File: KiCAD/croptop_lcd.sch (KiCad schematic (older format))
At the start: 73 parts, among them J4 54104-4031, U6 IS66WV51216EBLL, U7 BU21026MUV-E2

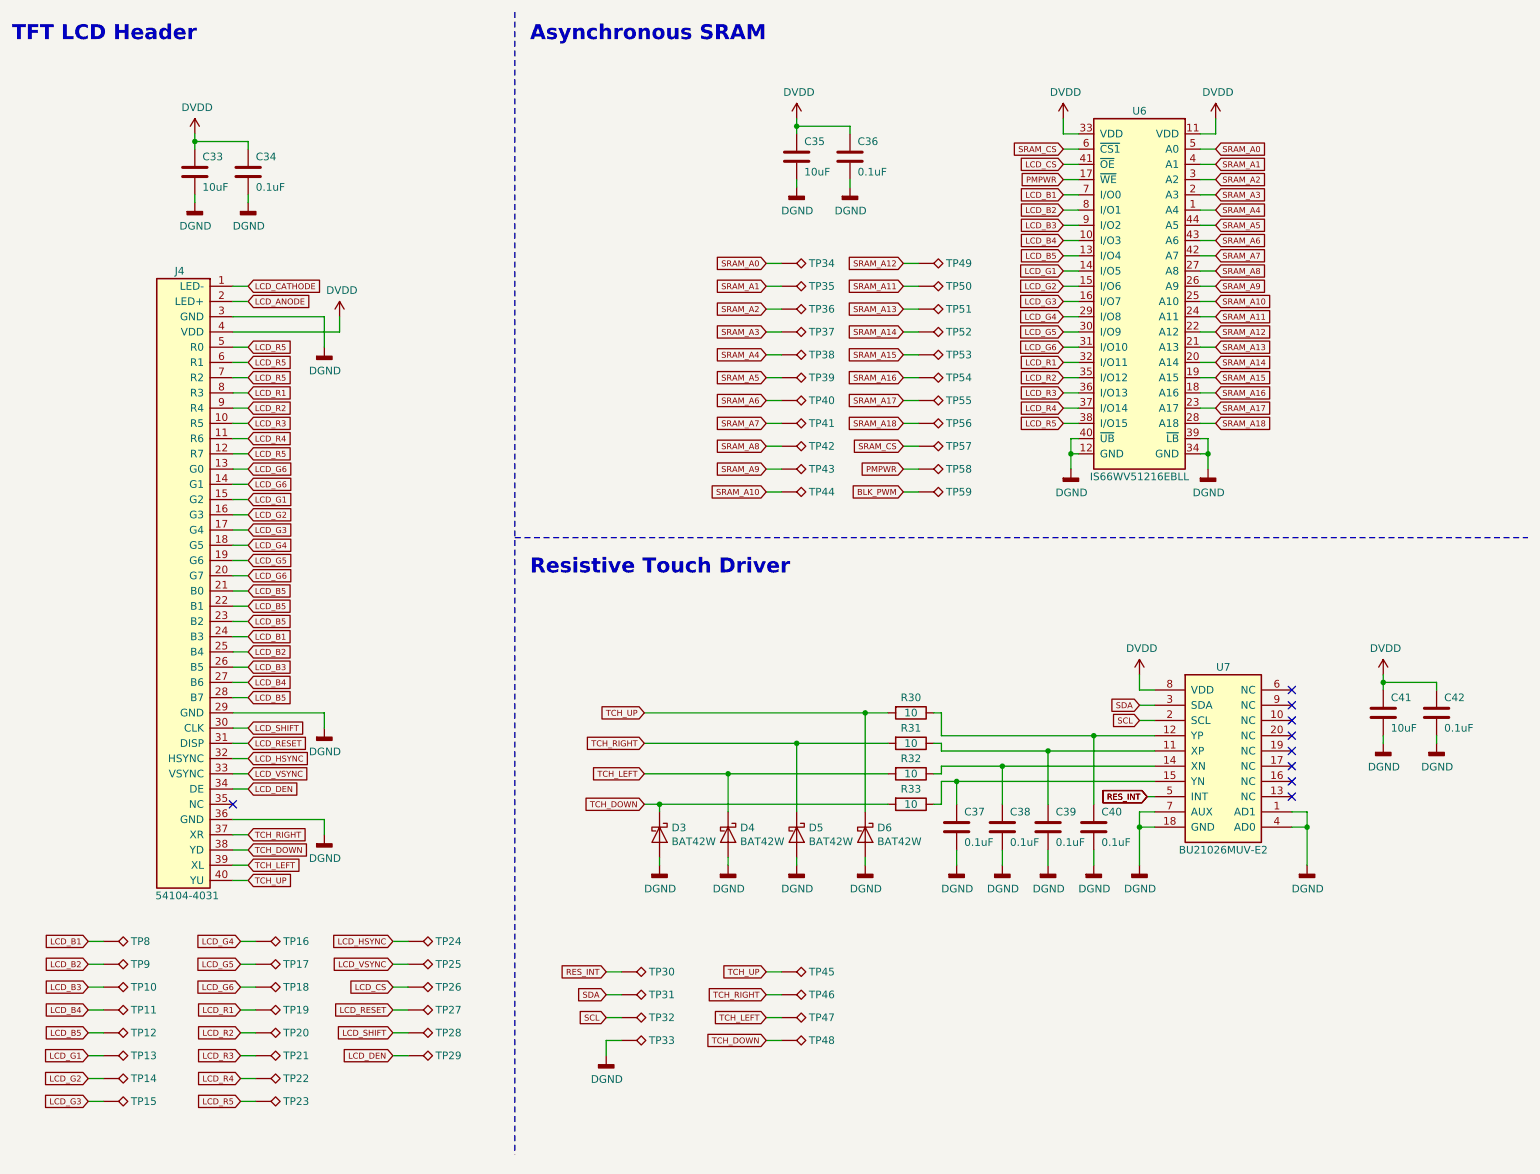
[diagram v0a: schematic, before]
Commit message: Got to PCB layout
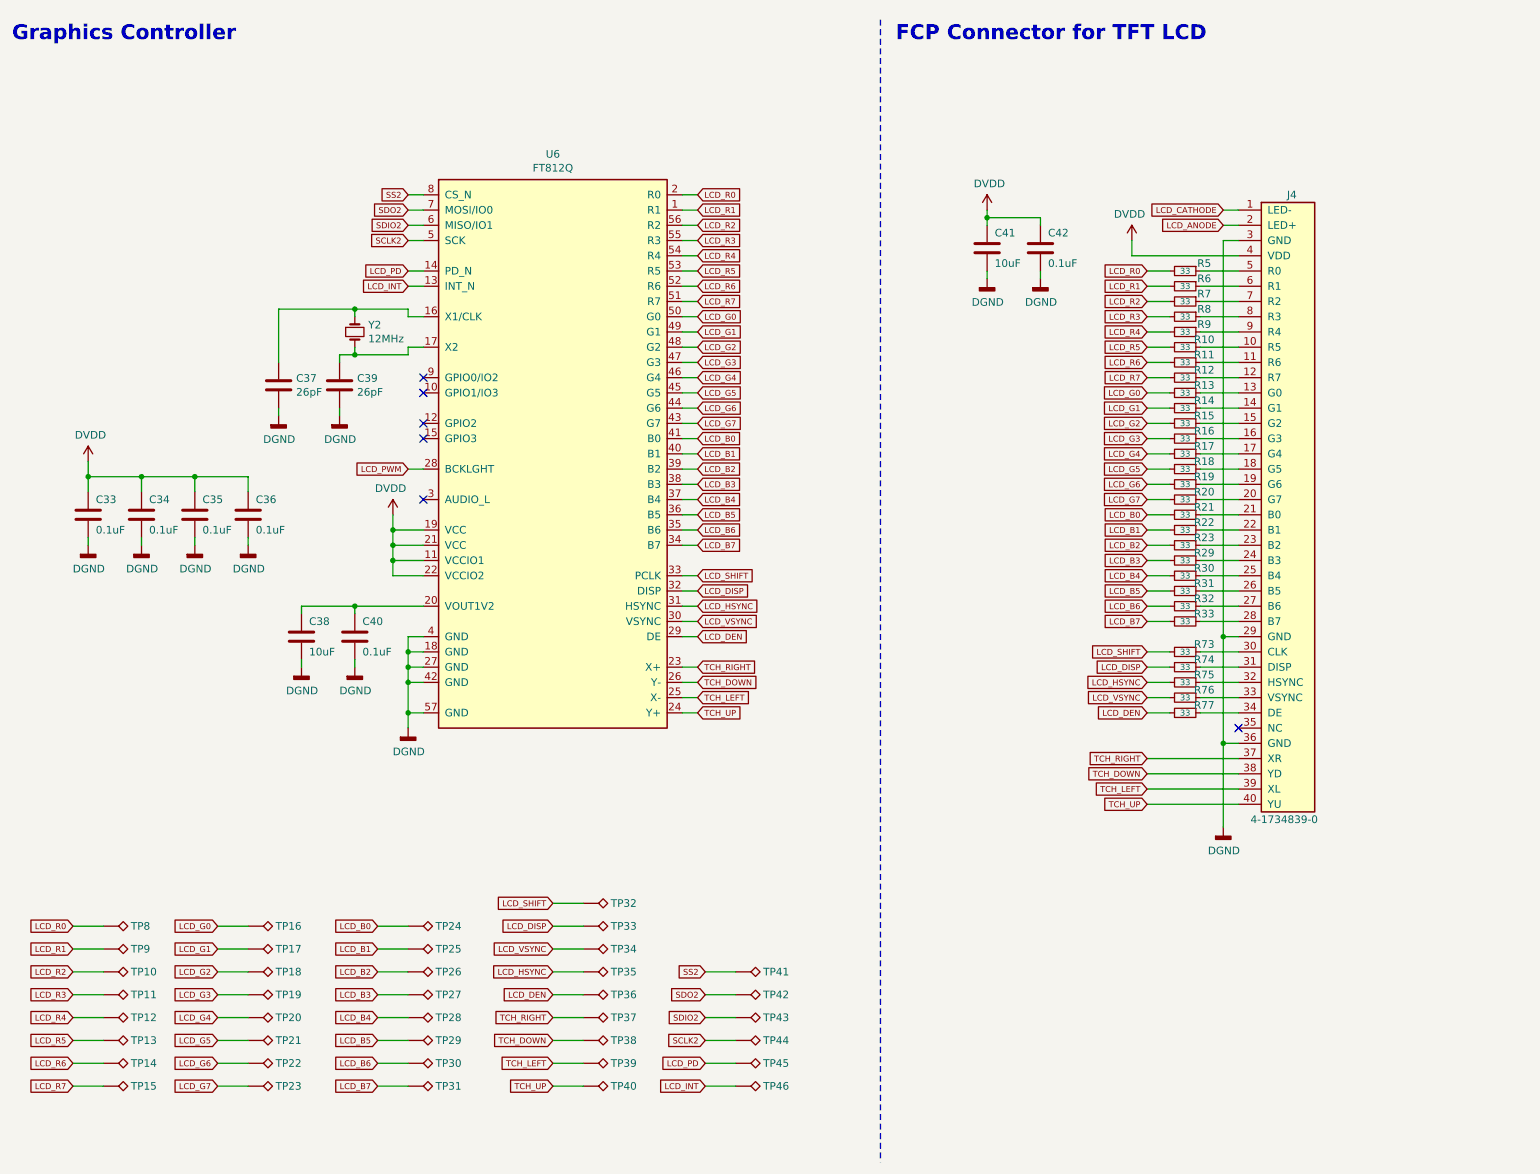
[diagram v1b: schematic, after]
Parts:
- removed D3, D4, D5, D6: BAT42W, symbol Device:D_Schottky
- removed R30, R31, R32, R33: 10, Resistor_SMD:R_0402_1005Metric, symbol Device:R
- removed TP47, TP48, TP49, TP50, TP51, TP52, TP53, TP54, TP55, TP56, TP57, TP58, TP59: TestPoint_Alt, TestPoint:TestPoint_Pad_D2.0mm, symbol Connector:TestPoint_Alt
- removed U6: IS66WV51216EBLL, Package_SO:TSOP-II-44_10.16x18.41mm_P0.8mm, symbol CropTop:IS66WV51216EBLL
- removed U7: BU21026MUV-E2, Package_DFN_QFN:VQFN-24-1EP_4x4mm_P0.5mm_EP2.45x2.45mm, symbol CropTop:BU21026MUV-E2
- added R10, R11, R12, R13, R14, R15, R16, R17, R18, R19, R20, R21, R22, R23, R29, R30, R31, R32, R33, R5, R6, R7, R73, R74, R75, R76, R77, R8, R9: 33, Resistor_SMD:R_0402_1005Metric, symbol Device:R_Small
- added U6: FT812Q, Package_DFN_QFN:QFN-56-1EP_8x8mm_P0.5mm_EP4.5x5.2mm, symbol CropTop:FT812Q
- added Y2: 12MHz, croptop:ABLS_OX, symbol Device:Crystal_Small
- C33, C35: value 10uF -> 0.1uF; footprint Capacitor_SMD:C_0805_2012Metric -> Capacitor_SMD:C_0402_1005Metric
- C37, C39: value 0.1uF -> 26pF
- C38: value 0.1uF -> 10uF; footprint Capacitor_SMD:C_0402_1005Metric -> Capacitor_SMD:C_0805_2012Metric
- J4: value 54104-4031 -> 4-1734839-0; footprint (none) -> croptop:4-1734839-0
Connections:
- net LCD_CS is gone; now on net LCD_B2: TP26.1
- net SCL is gone; now on net LCD_SHIFT: TP32.1
- net SRAM_A0 is gone; now on net LCD_VSYNC: TP34.1
- net SRAM_A1 is gone; now on net LCD_HSYNC: TP35.1
- net SRAM_A2 is gone; now on net LCD_DEN: TP36.1
- net SRAM_A3 is gone; now on net TCH_RIGHT: TP37.1
- net SRAM_A4 is gone; now on net TCH_DOWN: TP38.1
- net SRAM_A5 is gone; now on net TCH_LEFT: TP39.1
- net SRAM_A6 is gone; now on net TCH_UP: TP40.1
- net DGND: now also U6.18 (GND), U6.27 (GND), U6.4 (GND), U6.42 (GND), U6.57 (GND); no longer TP33.1
- net DVDD: now also U6.11 (VCCIO1), U6.19 (VCC), U6.21 (VCC), U6.22 (VCCIO2)
- net LCD_B1: now also TP25.1, R22.2, U6.40 (B1); no longer J4.24 (B3), TP8.1
- net LCD_B2: now also R23.2, U6.39 (B2); no longer J4.25 (B4), TP9.1
- net LCD_B3: now also TP27.1, R29.2, U6.38 (B3); no longer J4.26 (B5), TP10.1
- net LCD_B4: now also TP28.1, R30.2, U6.37 (B4); no longer J4.27 (B6), TP11.1
- net LCD_B5: now also TP29.1, R31.2, U6.36 (B5); no longer J4.21 (B0), J4.22 (B1), J4.23 (B2), J4.28 (B7), TP12.1
- net LCD_DEN: now also R77.2, U6.29 (DE); no longer J4.34 (DE), TP29.1
- net LCD_G1: now also TP17.1, R14.2, U6.49 (G1); no longer J4.15 (G2), TP13.1
- net LCD_G2: now also TP18.1, R15.2, U6.48 (G2); no longer J4.16 (G3), TP14.1
- net LCD_G3: now also TP19.1, R16.2, U6.47 (G3); no longer J4.17 (G4), TP15.1
- net LCD_G4: now also TP20.1, R17.2, U6.46 (G4); no longer J4.18 (G5), TP16.1
- net LCD_G5: now also TP21.1, R18.2, U6.45 (G5); no longer J4.19 (G6), TP17.1
- net LCD_G6: now also TP22.1, R19.2, U6.44 (G6); no longer J4.13 (G0), J4.14 (G1), J4.20 (G7), TP18.1
- net LCD_HSYNC: now also R75.2, U6.31 (HSYNC); no longer J4.32 (HSYNC), TP24.1
- net LCD_R1: now also TP9.1, R6.2, U6.1 (R1); no longer J4.8 (R3), TP19.1
- net LCD_R2: now also TP10.1, R7.2, U6.56 (R2); no longer J4.9 (R4), TP20.1
- net LCD_R3: now also TP11.1, R8.2, U6.55 (R3); no longer J4.10 (R5), TP21.1
- net LCD_R4: now also TP12.1, R9.2, U6.54 (R4); no longer J4.11 (R6), TP22.1
- net LCD_R5: now also TP13.1, R10.2, U6.53 (R5); no longer J4.12 (R7), J4.5 (R0), J4.6 (R1), J4.7 (R2), TP23.1
- net LCD_SHIFT: now also R73.2, U6.33 (PCLK); no longer J4.30 (CLK), TP28.1
- net LCD_VSYNC: now also R76.2, U6.30 (VSYNC); no longer J4.33 (VSYNC), TP25.1
- net TCH_DOWN: now also U6.26 (Y-)
- net TCH_LEFT: now also U6.25 (X-)
- net TCH_RIGHT: now also U6.23 (X+); no longer TP46.1
- net TCH_UP: now also U6.24 (Y+); no longer TP45.1
- net at C39.1: now also U6.17 (X2), Y2.2
- net at C40.1: now also C38.1, U6.20 (VOUT1V2)
- net at C37.1: now also U6.16 (X1/CLK), Y2.1
- net LCD_RESET: no longer names the net of J4.31 (DISP)
- net LCD_RESET: now also R74.1; no longer TP27.1
- net RES_INT renamed LCD_B6
- net LCD_B6: now also R32.2, U6.35 (B6)
- net SDA renamed LCD_B7
- net LCD_B7: now also R33.2, U6.34 (B7)
- net SRAM_A10 renamed SCLK2
- net SCLK2: now also U6.5 (SCK)
- net SRAM_A7 renamed SS2
- net SS2: now also U6.8 (CS_N)
- net SRAM_A8 renamed SDO2
- net SDO2: now also U6.7 (MOSI/IO0)
- net SRAM_A9 renamed SDIO2
- net SDIO2: now also U6.6 (MISO/IO1)
- new net: J4.10 (R5), R10.1
- new net: J4.11 (R6), R11.1
- new net: J4.12 (R7), R12.1
- new net: J4.13 (G0), R13.1
- new net: J4.14 (G1), R14.1
- new net: J4.15 (G2), R15.1
- new net: J4.16 (G3), R16.1
- new net: J4.17 (G4), R17.1
- new net: J4.18 (G5), R18.1
- new net: J4.19 (G6), R19.1
- new net: J4.20 (G7), R20.1
- new net: J4.21 (B0), R21.1
- new net: J4.22 (B1), R22.1
- new net: J4.23 (B2), R23.1
- new net: J4.24 (B3), R29.1
- new net: J4.25 (B4), R30.1
- new net: J4.26 (B5), R31.1
- new net: J4.27 (B6), R32.1
- new net: J4.28 (B7), R33.1
- new net: J4.30 (CLK), R73.1
- new net: J4.32 (HSYNC), R75.1
- new net: J4.33 (VSYNC), R76.1
- new net: J4.34 (DE), R77.1
- new net: J4.5 (R0), R5.1
- new net: J4.6 (R1), R6.1
- new net: J4.7 (R2), R7.1
- new net: J4.8 (R3), R8.1
- new net: J4.9 (R4), R9.1
- new net LCD_B0: R21.2, TP24.1, U6.41 (B0)
- new net LCD_DISP: R74.2, TP33.1, U6.32 (DISP)
- new net LCD_G0: R13.2, TP16.1, U6.50 (G0)
- new net LCD_G7: R20.2, TP23.1, U6.43 (G7)
- new net LCD_INT: TP46.1, U6.13 (INT_N)
- new net LCD_PD: TP45.1, U6.14 (PD_N)
- new net LCD_PWM: U6.28 (BCKLGHT)
- new net LCD_R0: R5.2, TP8.1, U6.2 (R0)
- new net LCD_R6: R11.2, TP14.1, U6.52 (R6)
- new net LCD_R7: R12.2, TP15.1, U6.51 (R7)
- no-connect marks 9 -> 6
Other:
- note added: "FCP Connector for TFT LCD"
- note added: "Graphics Controller"
- note removed: "Asynchronous SRAM"
- note removed: "Resistive Touch Driver"
- note removed: "TFT LCD Header"
- moved on the sheet: C41, C42, J4

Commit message: Before remove LCD resistors
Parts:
- removed C41: 10uF, Capacitor_SMD:C_0805_2012Metric, symbol Device:C
- removed C42: 0.1uF, Capacitor_SMD:C_0402_1005Metric, symbol Device:C
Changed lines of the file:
@@
-$EndComp
-$Comp
-L Device:C C?
-U 1 1 5C124BB4
-P 7300 2050
-AR Path="/5C124BB4" Ref="C?"  Part="1"
-AR Path="/65B709D0/5C124BB4" Ref="C42"  Part="1"
-AR Path="/66A12230/5C124BB4" Ref="C?"  Part="1"
-AR Path="/669AB112/5C124BB4" Ref="C?"  Part="1"
-F 0 "C42" H 7350 2150 50  0000 L CNN
-F 1 "0.1uF" H 7350 1950 50  0000 L CNN
-F 2 "Capacitor_SMD:C_0402_1005Metric" H 7338 1900 50  0001 C CNN
-F 3 "~" H 7300 2050 50  0001 C CNN
-	1    7300 2050
-	1    0    0    -1
-$EndComp
-$Comp
-L Device:C C?
-U 1 1 5C124BBB
-P 6950 2050
-AR Path="/5C124BBB" Ref="C?"  Part="1"
-AR Path="/65B709D0/5C124BBB" Ref="C41"  Part="1"
-AR Path="/66A12230/5C124BBB" Ref="C?"  Part="1"
-AR Path="/669AB112/5C124BBB" Ref="C?"  Part="1"
-F 0 "C41" H 7000 2150 50  0000 L CNN
-F 1 "10uF" H 7000 1950 50  0000 L CNN
-F 2 "Capacitor_SMD:C_0805_2012Metric" H 6988 1900 50  0001 C CNN
-F 3 "~" H 6950 2050 50  0001 C CNN
-	1    6950 2050
-	1    0    0    -1
-$EndComp
-Wire Wire Line
-	7300 1900 7300 1850
-Wire Wire Line
-	6950 2250 6950 2200
-Wire Wire Line
-	7300 2250 7300 2200
-Wire Wire Line
-	6950 1900 6950 1850
-Wire Wire Line
-	6950 1800 6950 1850
-Connection ~ 6950 1850
-$Comp
-L CropTop:DGND #PWR085
-U 1 1 5C124BC8
-P 7300 2250
-F 0 "#PWR085" H 7300 2000 50  0001 C CNN
-F 1 "DGND" H 7304 2095 50  0000 C CNN
-F 2 "" H 7300 2250 50  0001 C CNN
-F 3 "" H 7300 2250 50  0001 C CNN
-	1    7300 2250
-	1    0    0    -1
-$EndComp
-Wire Wire Line
-	6950 1850 7300 1850
-$Comp
-L CropTop:DVDD #PWR083
-U 1 1 5C124BCF
-P 6950 1800
-F 0 "#PWR083" H 6950 1650 50  0001 C CNN
-F 1 "DVDD" H 6965 1973 50  0000 C CNN
-F 2 "" H 6950 1800 50  0001 C CNN
-F 3 "" H 6950 1800 50  0001 C CNN
-	1    6950 1800
-	1    0    0    -1
-$EndComp
-$Comp
-L CropTop:DGND #PWR084
-U 1 1 5C124BD5
-P 6950 2250
-F 0 "#PWR084" H 6950 2000 50  0001 C CNN
-F 1 "DGND" H 6954 2095 50  0000 C CNN
-F 2 "" H 6950 2250 50  0001 C CNN
-F 3 "" H 6950 2250 50  0001 C CNN
-	1    6950 2250
-	1    0    0    -1
 $EndComp
 $Comp

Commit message: Changed testpoint size
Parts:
- TP10, TP11, TP12, TP13, TP14, TP15, TP16, TP17, TP18, TP19, TP20, TP21, TP22, TP23, TP24, TP25, TP26, TP27, TP28, TP29, TP30, TP31, TP32, TP33, TP34, TP35, TP36, TP37, TP38, TP39, TP40, TP41, TP42, TP43, TP44, TP45, TP46, TP8, TP9: footprint TestPoint:TestPoint_Pad_D2.0mm -> TestPoint:TestPoint_Pad_1.0x1.0mm

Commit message: Complete PCB version 1
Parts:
- R10, R11, R12, R13, R14, R15, R16, R17, R18, R19, R20, R21, R22, R23, R29, R30, R31, R32, R33, R5, R6, R7, R73, R74, R75, R76, R77, R8, R9: value 33 -> 22
- TP10, TP11, TP12, TP13, TP14, TP15, TP16, TP17, TP18, TP19, TP20, TP21, TP22, TP23, TP24, TP25, TP26, TP27, TP28, TP29, TP30, TP31, TP32, TP33, TP34, TP35, TP36, TP37, TP38, TP39, TP40, TP41, TP42, TP43, TP44, TP45, TP46, TP8, TP9: footprint TestPoint:TestPoint_Pad_1.0x1.0mm -> croptop:TestPoint
